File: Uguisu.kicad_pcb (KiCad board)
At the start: 2 copper layers, 35 x 50 mm, 8 parts, among them U1 XIAO-nRF52840-SMD

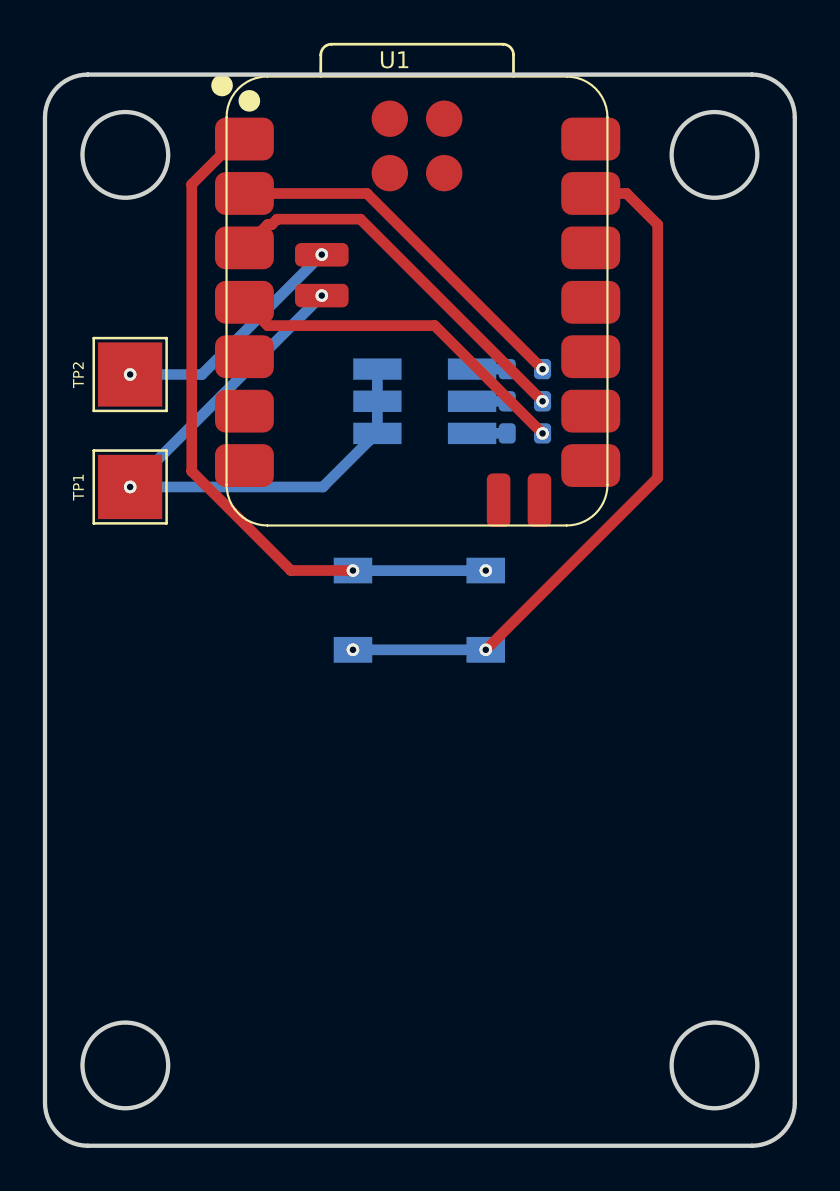
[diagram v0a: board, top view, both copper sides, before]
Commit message: LED pin order and docs: D1=Blue, D2=Red, D3=Green; R1=Blue, R2=Red, R3=Green; LED1 pins 1/2/3
Made-with: Cursor
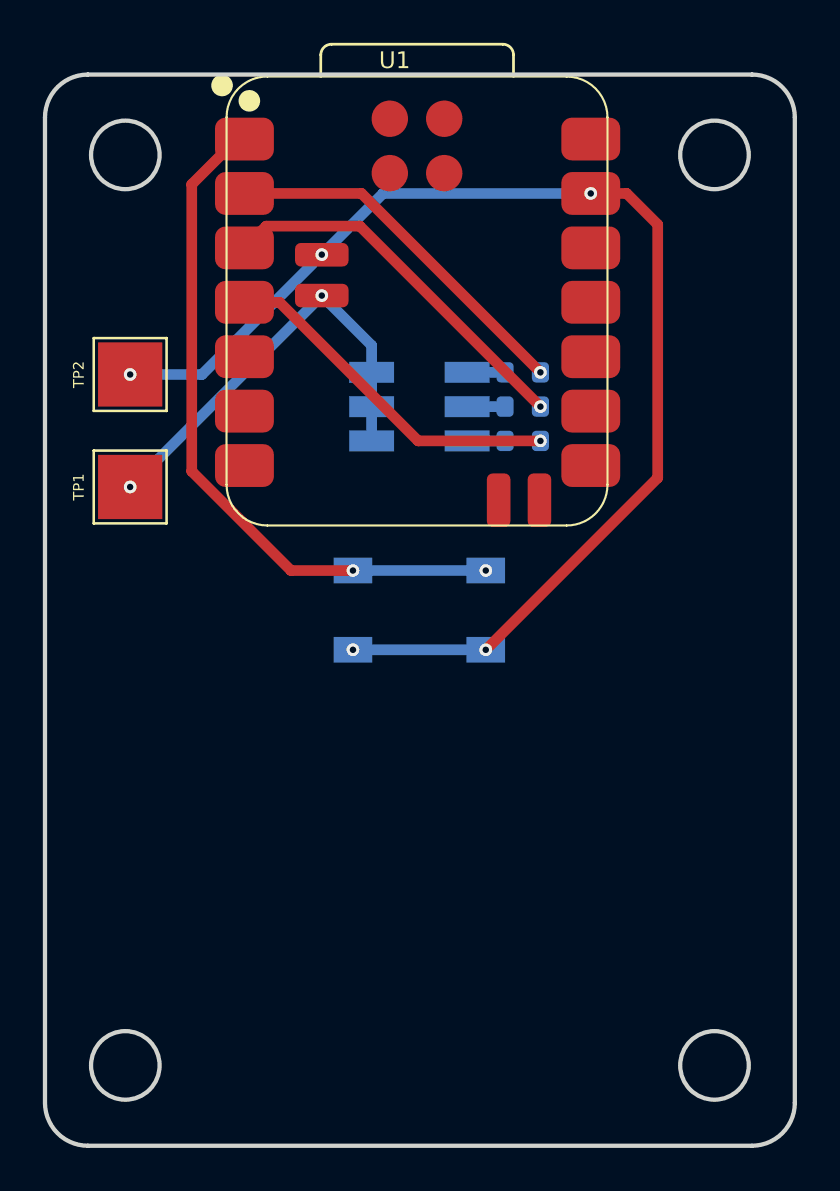
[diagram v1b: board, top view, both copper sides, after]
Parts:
- LED1: value TC5050RGBF08-3CJH-AF53A -> XL-5050RGBC; footprint easyeda2kicad:LED-SMD_6P-L5.0-W5.0-TL_TC5050RGBF08 -> easyeda2kicad:LED-ARRAY-SMD_6P-L5.0-W5.0-TL-RD_3
- R3: value 150 -> 120
- moved R3 0.36 mm to (123.8, 77.8)
- moved LED1 0.35 mm to (119.0, 76.2), turned to 180 degrees
- moved R2 0.27 mm to (123.8, 76.2)
- moved R1 0.18 mm to (123.8, 74.7)
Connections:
- LED1 pad 1: +BATT -> Net-(LED1-B-)
- LED1 pad 2: +BATT -> Net-(LED1-R-)
- LED1 pad 3: +BATT -> Net-(LED1-G-)
- LED1 pad 4: Net-(LED1---Pad4) -> +BATT
- LED1 pad 5: Net-(LED1---Pad5) -> +BATT
- LED1 pad 6: Net-(LED1---Pad6) -> +BATT
- R1 pad 1: Net-(LED1---Pad4) -> Net-(LED1-B-)
- R2 pad 1: Net-(LED1---Pad5) -> Net-(LED1-R-)
- R3 pad 2: Net-(LED1---Pad6) -> Net-(LED1-G-)
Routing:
- net GND: track 44.4 -> 58.1 mm, vias 4 -> 5
- net +BATT: track 28.3 -> 20.4 mm
- net Net-(LED1-R-): track 0.00 -> 1.77 mm
- net Net-(LED1-G-): track 0.00 -> 1.77 mm
- net Net-(LED1-B-): track 0.00 -> 1.77 mm
- net Net-(LED1---Pad6): track 1.64 -> 0.00 mm
- net Net-(LED1---Pad5): track 1.64 -> 0.00 mm
- net Net-(LED1---Pad4): track 1.64 -> 0.00 mm
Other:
- outline, holes or cut-outs redrawn

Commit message: pcb: adjust routing and via positions
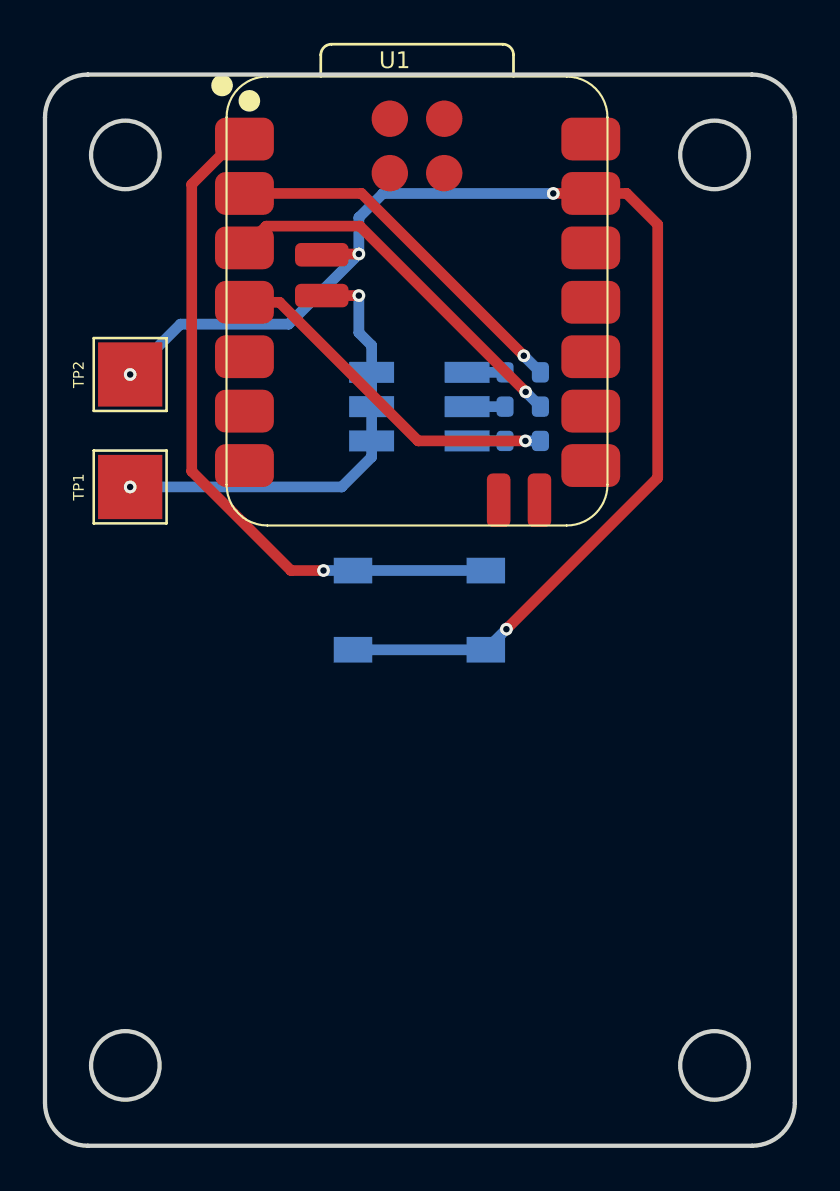
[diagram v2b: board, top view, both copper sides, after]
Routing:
- net GND: track 58.1 -> 60.9 mm, vias 5 -> 4
- net +BATT: track 20.4 -> 21.4 mm
- net /MCU_D0: vias 2 -> 1
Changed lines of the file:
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@@
 	)
 	(segment
-		(start 124.65 74.65)
+		(start 123.875 73.875)
 		(end 116.3 66.3)
 		(width 0.5)
@@
 	)
 	(via
-		(at 124.65 74.65)
+		(at 123.875 73.875)
 		(size 0.6)
 		(drill 0.3)
@@
 	)
 	(segment
+		(start 123.875 73.875)
+		(end 124.65 74.65)
+		(width 0.5)
+		(layer "B.Cu")
+		(net 1)
+	)
+	(segment
+		(start 125.25 66.3)
+		(end 128.675 66.3)
+		(width 0.5)
+		(layer "F.Cu")
+		(net 2)
+	)
+	(segment
+		(start 114.475 69.125)
+		(end 114.45 69.15)
+		(width 0.5)
+		(layer "F.Cu")
+		(net 2)
+	)
+	(segment
+		(start 116.175 69.125)
+		(end 114.4815 69.125)
+		(width 0.5)
+		(layer "F.Cu")
+		(net 2)
+	)
+	(segment
+		(start 116.1385 69.1615)
+		(end 116.175 69.125)
+		(width 0.5)
+		(layer "F.Cu")
+		(net 2)
+	)
+	(segment
+		(start 130.125 67.75)
+		(end 130.125 79.575)
+		(width 0.5)
+		(layer "F.Cu")
+		(net 2)
+	)
+	(segment
+		(start 114.4815 69.125)
+		(end 114.445 69.1615)
+		(width 0.5)
+		(layer "F.Cu")
+		(net 2)
+	)
+	(segment
 		(start 128.675 66.3)
-		(end 127 66.3)
-		(width 0.5)
-		(layer "F.Cu")
-		(net 2)
-	)
-	(segment
-		(start 114.445 69.155)
-		(end 114.45 69.15)
-		(width 0.5)
-		(layer "F.Cu")
-		(net 2)
-	)
-	(segment
-		(start 130.125 67.75)
-		(end 128.675 66.3)
+		(end 130.125 67.75)
 		(width 0.5)
 		(layer "F.Cu")
@@
 	(segment
 		(start 130.125 79.575)
-		(end 130.125 67.75)
-		(width 0.5)
-		(layer "F.Cu")
-		(net 2)
-	)
-	(segment
-		(start 122.1 87.6)
-		(end 130.125 79.575)
-		(width 0.5)
-		(layer "F.Cu")
-		(net 2)
-	)
-	(segment
-		(start 114.445 69.1615)
-		(end 114.445 69.155)
-		(width 0.5)
-		(layer "F.Cu")
-		(net 2)
-	)
-	(via
-		(at 122.1 87.6)
-		(size 0.6)
-		(drill 0.3)
-		(layers "F.Cu" "B.Cu")
-		(net 2)
-	)
-	(via
-		(at 114.445 69.155)
-		(size 0.6)
-		(drill 0.3)
-		(layers "F.Cu" "B.Cu")
-		(net 2)
-	)
-	(via
-		(at 127 66.3)
-		(size 0.6)
-		(drill 0.3)
-		(layers "F.Cu" "B.Cu")
-		(net 2)
-	)
-	(via
-		(at 115.9 87.6)
+		(end 123.0625 86.6375)
+		(width 0.5)
+		(layer "F.Cu")
+		(net 2)
+	)
+	(via
+		(at 123.0625 86.6375)
+		(size 0.6)
+		(drill 0.3)
+		(layers "F.Cu" "B.Cu")
+		(net 2)
+	)
+	(via
+		(at 116.175 69.125)
+		(size 0.6)
+		(drill 0.3)
+		(layers "F.Cu" "B.Cu")
+		(net 2)
+	)
+	(via
+		(at 125.25 66.3)
 		(size 0.6)
 		(drill 0.3)
@@
 	)
 	(segment
+		(start 115.9 87.6)
+		(end 122.1 87.6)
+		(width 0.5)
+		(layer "B.Cu")
+		(net 2)
+	)
+	(segment
+		(start 107.85 72.4)
+		(end 112.9 72.4)
+		(width 0.5)
+		(layer "B.Cu")
+		(net 2)
+	)
+	(segment
+		(start 123.0625 86.6375)
+		(end 122.1 87.6)
+		(width 0.5)
+		(layer "B.Cu")
+		(net 2)
+	)
+	(segment
+		(start 112.9 72.4)
+		(end 116.175 69.125)
+		(width 0.5)
+		(layer "B.Cu")
+		(net 2)
+	)
+	(segment
+		(start 105.5 74.75)
+		(end 107.85 72.4)
+		(width 0.5)
+		(layer "B.Cu")
+		(net 2)
+	)
+	(segment
+		(start 125.25 66.3)
+		(end 117.3 66.3)
+		(width 0.5)
+		(layer "B.Cu")
+		(net 2)
+	)
+	(segment
+		(start 116.175 67.425)
+		(end 116.175 69.125)
+		(width 0.5)
+		(layer "B.Cu")
+		(net 2)
+	)
+	(segment
 		(start 117.3 66.3)
-		(end 127 66.3)
-		(width 0.5)
-		(layer "B.Cu")
-		(net 2)
-	)
-	(segment
-		(start 114.445 69.155)
-		(end 108.85 74.75)
-		(width 0.5)
-		(layer "B.Cu")
-		(net 2)
-	)
-	(segment
-		(start 114.445 69.155)
-		(end 117.3 66.3)
-		(width 0.5)
-		(layer "B.Cu")
-		(net 2)
-	)
-	(segment
-		(start 108.85 74.75)
-		(end 105.5 74.75)
-		(width 0.5)
-		(layer "B.Cu")
-		(net 2)
-	)
-	(segment
-		(start 122.1 87.6)
-		(end 115.9 87.6)
+		(end 116.175 67.425)
 		(width 0.5)
 		(layer "B.Cu")
@@
 	)
 	(segment
-		(start 114.445 71.0665)
-		(end 114.4235 71.0665)
-		(width 0.5)
-		(layer "F.Cu")
-		(net 12)
-	)
-	(via
-		(at 114.445 71.0665)
+		(start 116.175 71.0665)
+		(end 114.445 71.0665)
+		(width 0.5)
+		(layer "F.Cu")
+		(net 12)
+	)
+	(via
+		(at 116.175 71.0665)
 		(size 0.6)
 		(drill 0.3)
@@
 	)
 	(segment
-		(start 114.445 71.0665)
+		(start 116.77 78.605)
+		(end 116.77 77.85)
+		(width 0.5)
+		(layer "B.Cu")
+		(net 12)
+	)
+	(segment
+		(start 115.375 80)
+		(end 116.77 78.605)
+		(width 0.5)
+		(layer "B.Cu")
+		(net 12)
+	)
+	(segment
+		(start 116.175 72.7965)
 		(end 116.77 73.3915)
 		(width 0.5)
@@
 	)
 	(segment
-		(start 105.5 80)
-		(end 105.5115 80)
-		(width 0.5)
-		(layer "B.Cu")
-		(net 12)
-	)
-	(segment
-		(start 105.5115 80)
-		(end 114.445 71.0665)
+		(start 116.175 71.0665)
+		(end 116.175 72.7965)
 		(width 0.5)
 		(layer "B.Cu")
@@
 	)
 	(segment
+		(start 105.5 80)
+		(end 115.375 80)
+		(width 0.5)
+		(layer "B.Cu")
+		(net 12)
+	)
+	(segment
 		(start 108.375 65.875)
 		(end 110.49 63.76)
@@
 	)
 	(segment
+		(start 114.525 83.9)
+		(end 113.00781 83.9)
+		(width 0.5)
+		(layer "F.Cu")
+		(net 13)
+	)
+	(segment
+		(start 110.49 63.76)
+		(end 110.835 63.76)
+		(width 0.5)
+		(layer "F.Cu")
+		(net 13)
+	)
+	(segment
+		(start 113.00781 83.9)
+		(end 108.375 79.26719)
+		(width 0.5)
+		(layer "F.Cu")
+		(net 13)
+	)
+	(segment
 		(start 108.375 79.26719)
 		(end 108.375 65.875)
@@
 		(net 13)
 	)
-	(segment
-		(start 115.9 83.9)
-		(end 113.00781 83.9)
-		(width 0.5)
-		(layer "F.Cu")
-		(net 13)
-	)
-	(segment
-		(start 113.00781 83.9)
-		(end 108.375 79.26719)
-		(width 0.5)
-		(layer "F.Cu")
-		(net 13)
-	)
-	(segment
-		(start 110.49 63.76)
-		(end 110.835 63.76)
-		(width 0.5)
-		(layer "F.Cu")
-		(net 13)
-	)
-	(via
-		(at 122.1 83.9)
-		(size 0.6)
-		(drill 0.3)
-		(layers "F.Cu" "B.Cu")
-		(net 13)
-	)
-	(via
-		(at 115.9 83.9)
-		(size 0.6)
-		(drill 0.3)
-		(layers "F.Cu" "B.Cu")
-		(net 13)
-	)
-	(segment
-		(start 115.9 83.9)
+	(via
+		(at 114.525 83.9)
+		(size 0.6)
+		(drill 0.3)
+		(layers "F.Cu" "B.Cu")
+		(net 13)
+	)
+	(segment
+		(start 114.525 83.9)
 		(end 122.1 83.9)
 		(width 0.5)
 		(layer "B.Cu")
 		(net 13)
+	)
+	(segment
+		(start 116.225 67.825)
+		(end 111.85 67.825)
+		(width 0.5)
+		(layer "F.Cu")
+		(net 14)
 	)
 	(segment
@@
 	)
 	(segment
-		(start 124.65 76.25)
+		(start 123.9625 75.5625)
 		(end 116.225 67.825)
 		(width 0.5)
@@
 		(net 14)
 	)
-	(segment
-		(start 116.225 67.825)
-		(end 111.85 67.825)
-		(width 0.5)
-		(layer "F.Cu")
-		(net 14)
-	)
-	(via
-		(at 124.65 76.25)
-		(size 0.6)
-		(drill 0.3)
-		(layers "F.Cu" "B.Cu")
+	(via
+		(at 123.9625 75.5625)
+		(size 0.6)
+		(drill 0.3)
+		(layers "F.Cu" "B.Cu")
+		(net 14)
+	)
+	(segment
+		(start 123.9625 75.5625)
+		(end 124.65 76.25)
+		(width 0.5)
+		(layer "B.Cu")
 		(net 14)
 	)
@@
 	)
 	(segment
-		(start 124.65 77.85)
-		(end 118.944162 77.85)
-		(width 0.5)
-		(layer "F.Cu")
-		(net 15)
-	)
-	(segment
 		(start 112.474162 71.38)
 		(end 110.835 71.38)
@@
 		(net 15)
 	)
-	(via
-		(at 124.65 77.85)
-		(size 0.6)
-		(drill 0.3)
-		(layers "F.Cu" "B.Cu")
-		(net 15)
-	)
+	(segment
+		(start 123.95 77.85)
+		(end 118.944162 77.85)
+		(width 0.5)
+		(layer "F.Cu")
+		(net 15)
+	)
+	(via
+		(at 123.95 77.85)
+		(size 0.6)
+		(drill 0.3)
+		(layers "F.Cu" "B.Cu")
+		(net 15)
+	)
+	(segment
+		(start 123.95 77.85)
+		(end 124.65 77.85)
+		(width 0.5)
+		(layer "B.Cu")
+		(net 15)
+	)
